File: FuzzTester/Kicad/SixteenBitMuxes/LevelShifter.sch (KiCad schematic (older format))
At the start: 6 parts, among them U22 4504, U23 4504, U24 4504

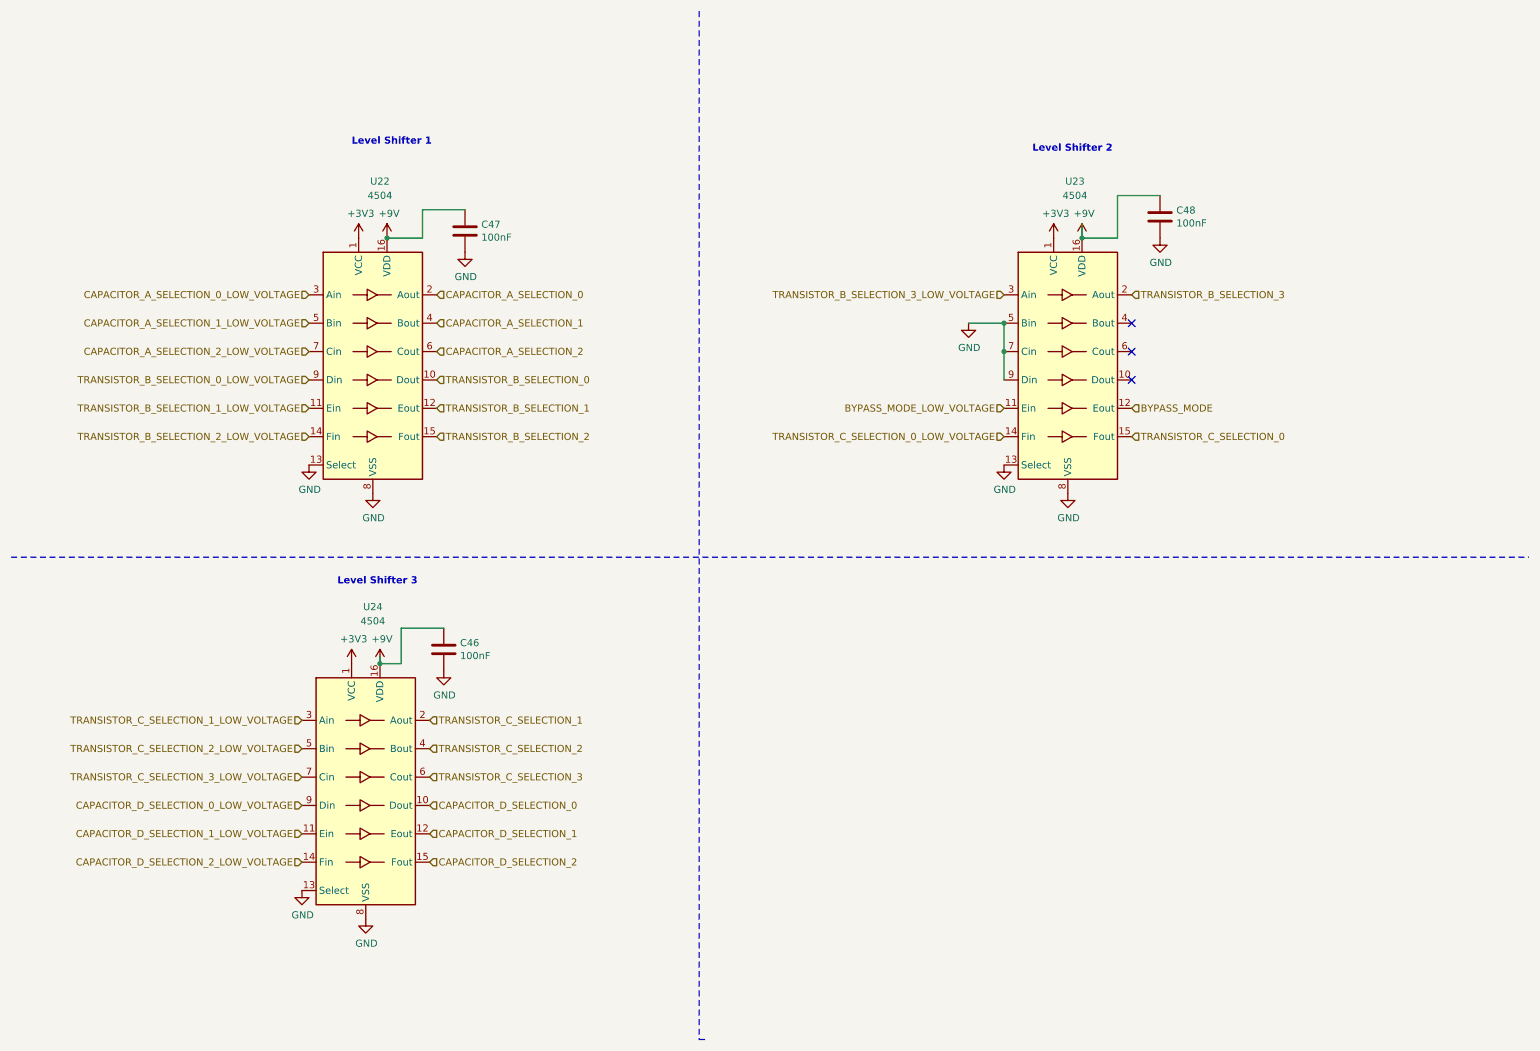
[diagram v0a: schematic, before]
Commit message: Removed shift registers
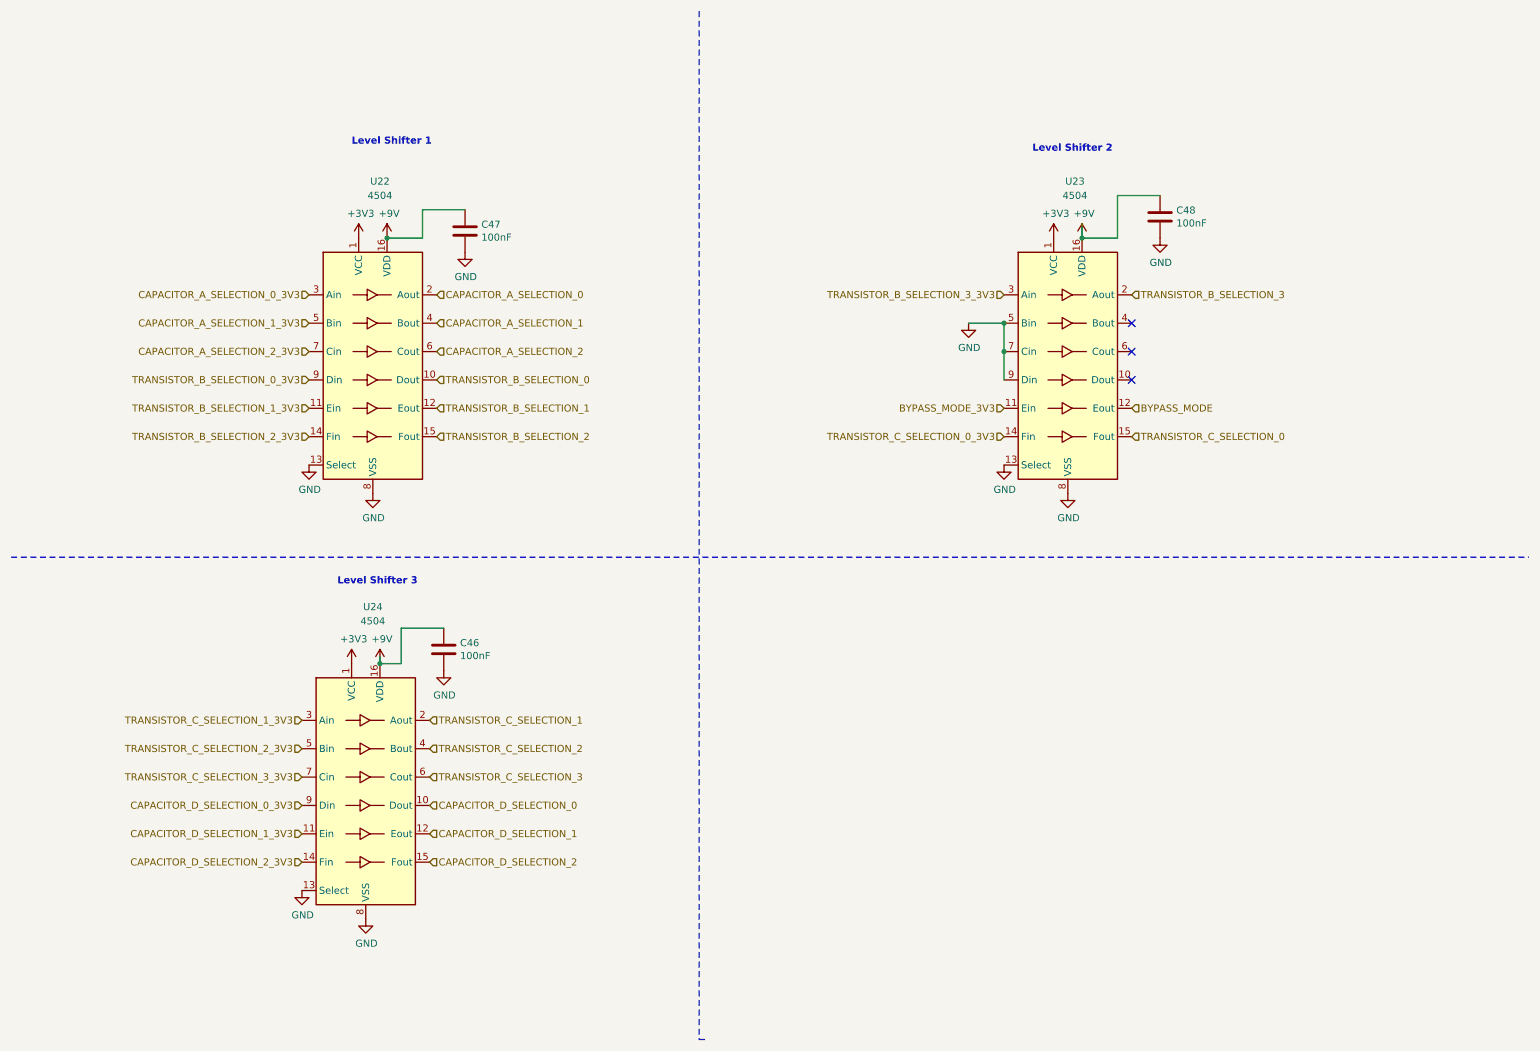
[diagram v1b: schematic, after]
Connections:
- net labels added: BYPASS_MODE_3V3, CAPACITOR_A_SELECTION_0_3V3, CAPACITOR_A_SELECTION_1_3V3, CAPACITOR_A_SELECTION_2_3V3, CAPACITOR_D_SELECTION_0_3V3, CAPACITOR_D_SELECTION_1_3V3, CAPACITOR_D_SELECTION_2_3V3, TRANSISTOR_B_SELECTION_0_3V3, TRANSISTOR_B_SELECTION_1_3V3, TRANSISTOR_B_SELECTION_2_3V3, TRANSISTOR_B_SELECTION_3_3V3, TRANSISTOR_C_SELECTION_0_3V3, TRANSISTOR_C_SELECTION_1_3V3, TRANSISTOR_C_SELECTION_2_3V3, TRANSISTOR_C_SELECTION_3_3V3
- net labels removed: BYPASS_MODE_LOW_VOLTAGE, CAPACITOR_A_SELECTION_0_LOW_VOLTAGE, CAPACITOR_A_SELECTION_1_LOW_VOLTAGE, CAPACITOR_A_SELECTION_2_LOW_VOLTAGE, CAPACITOR_D_SELECTION_0_LOW_VOLTAGE, CAPACITOR_D_SELECTION_1_LOW_VOLTAGE, CAPACITOR_D_SELECTION_2_LOW_VOLTAGE, TRANSISTOR_B_SELECTION_0_LOW_VOLTAGE, TRANSISTOR_B_SELECTION_1_LOW_VOLTAGE, TRANSISTOR_B_SELECTION_2_LOW_VOLTAGE, TRANSISTOR_B_SELECTION_3_LOW_VOLTAGE, TRANSISTOR_C_SELECTION_0_LOW_VOLTAGE, TRANSISTOR_C_SELECTION_1_LOW_VOLTAGE, TRANSISTOR_C_SELECTION_2_LOW_VOLTAGE, TRANSISTOR_C_SELECTION_3_LOW_VOLTAGE
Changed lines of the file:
@@
 $Descr A4 11693 8268
 encoding utf-8
-Sheet 11 11
+Sheet 11 9
 Title ""
 Date ""
@@
 	3250 5100 3100 5100
 Text HLabel 7500 3300 0    50   Input ~ 0
-BYPASS_MODE_LOW_VOLTAGE
+BYPASS_MODE_3V3
 Wire Wire Line
 	7250 2700 7500 2700
@@
 NoConn ~ 8400 3100
 Text HLabel 2600 2500 0    50   Input ~ 0
-CAPACITOR_A_SELECTION_0_LOW_VOLTAGE
+CAPACITOR_A_SELECTION_0_3V3
 Text HLabel 2600 2700 0    50   Input ~ 0
-CAPACITOR_A_SELECTION_1_LOW_VOLTAGE
+CAPACITOR_A_SELECTION_1_3V3
 Text HLabel 2600 2900 0    50   Input ~ 0
-CAPACITOR_A_SELECTION_2_LOW_VOLTAGE
+CAPACITOR_A_SELECTION_2_3V3
 Text HLabel 2600 3100 0    50   Input ~ 0
-TRANSISTOR_B_SELECTION_0_LOW_VOLTAGE
+TRANSISTOR_B_SELECTION_0_3V3
 Text HLabel 2600 3300 0    50   Input ~ 0
-TRANSISTOR_B_SELECTION_1_LOW_VOLTAGE
+TRANSISTOR_B_SELECTION_1_3V3
 Text HLabel 2600 3500 0    50   Input ~ 0
-TRANSISTOR_B_SELECTION_2_LOW_VOLTAGE
+TRANSISTOR_B_SELECTION_2_3V3
 Text HLabel 7500 2500 0    50   Input ~ 0
-TRANSISTOR_B_SELECTION_3_LOW_VOLTAGE
+TRANSISTOR_B_SELECTION_3_3V3
 Text HLabel 8400 2500 2    50   Input ~ 0
 TRANSISTOR_B_SELECTION_3
 Text HLabel 7500 3500 0    50   Input ~ 0
-TRANSISTOR_C_SELECTION_0_LOW_VOLTAGE
+TRANSISTOR_C_SELECTION_0_3V3
 Text HLabel 8400 3500 2    50   Input ~ 0
 TRANSISTOR_C_SELECTION_0
 Text HLabel 2550 6500 0    50   Input ~ 0
-CAPACITOR_D_SELECTION_2_LOW_VOLTAGE
+CAPACITOR_D_SELECTION_2_3V3
 Text HLabel 2550 6300 0    50   Input ~ 0
-CAPACITOR_D_SELECTION_1_LOW_VOLTAGE
+CAPACITOR_D_SELECTION_1_3V3
 Text HLabel 2550 6100 0    50   Input ~ 0
-CAPACITOR_D_SELECTION_0_LOW_VOLTAGE
+CAPACITOR_D_SELECTION_0_3V3
 Text HLabel 2550 5700 0    50   Input ~ 0
-TRANSISTOR_C_SELECTION_2_LOW_VOLTAGE
+TRANSISTOR_C_SELECTION_2_3V3
 Text HLabel 2550 5500 0    50   Input ~ 0
-TRANSISTOR_C_SELECTION_1_LOW_VOLTAGE
+TRANSISTOR_C_SELECTION_1_3V3
 Text HLabel 3450 5900 2    50   Input ~ 0
 TRANSISTOR_C_SELECTION_3
 Text HLabel 2550 5900 0    50   Input ~ 0
-TRANSISTOR_C_SELECTION_3_LOW_VOLTAGE
+TRANSISTOR_C_SELECTION_3_3V3
 $EndSCHEMATC

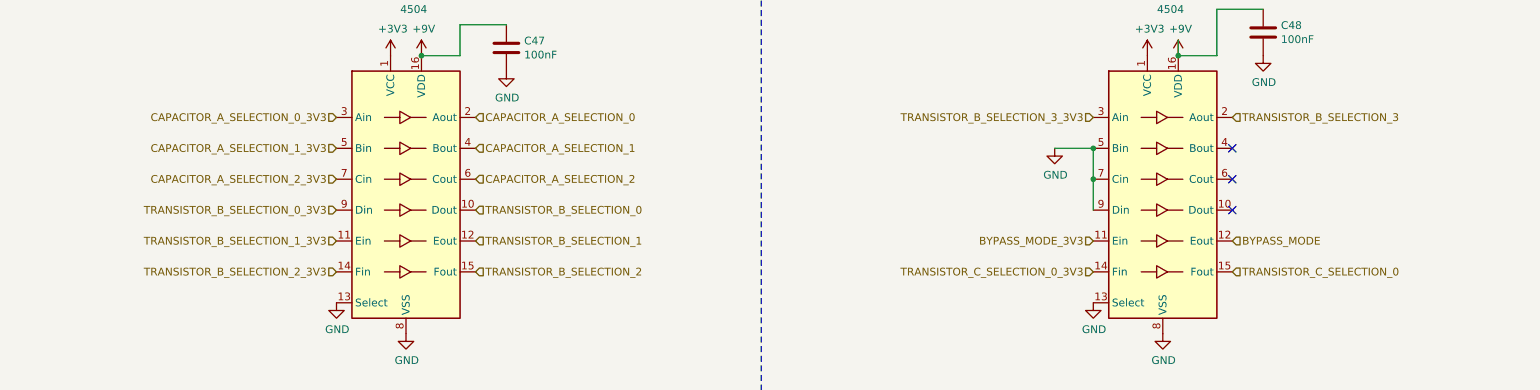
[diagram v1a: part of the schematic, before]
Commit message: Finished (but not beautiful) PCB without SPI and most 8 channel multiplexers.
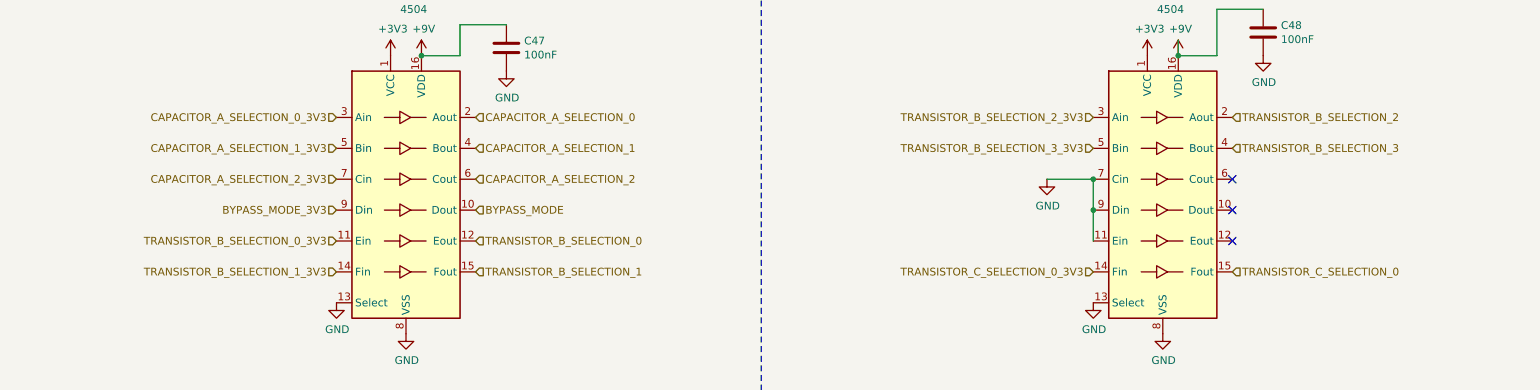
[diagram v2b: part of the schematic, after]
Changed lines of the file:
@@
 $Descr A4 11693 8268
 encoding utf-8
-Sheet 11 9
+Sheet 9 9
 Title ""
 Date ""
@@
 Text HLabel 3500 2900 2    50   Input ~ 0
 CAPACITOR_A_SELECTION_2
-Text HLabel 3500 3100 2    50   Input ~ 0
+Text HLabel 3500 3300 2    50   Input ~ 0
 TRANSISTOR_B_SELECTION_0
-Text HLabel 3500 3300 2    50   Input ~ 0
+Text HLabel 3500 3500 2    50   Input ~ 0
 TRANSISTOR_B_SELECTION_1
-Text HLabel 3500 3500 2    50   Input ~ 0
+Text HLabel 8400 2500 2    50   Input ~ 0
 TRANSISTOR_B_SELECTION_2
 $Comp
@@
 L power:GND #PWR0125
 U 1 1 5EDC2DD2
-P 7250 2700
-F 0 "#PWR0125" H 7250 2450 50  0001 C CNN
-F 1 "GND" H 7255 2527 50  0000 C CNN
-F 2 "" H 7250 2700 50  0001 C CNN
-F 3 "" H 7250 2700 50  0001 C CNN
-	1    7250 2700
+P 7200 2900
+F 0 "#PWR0125" H 7200 2650 50  0001 C CNN
+F 1 "GND" H 7205 2727 50  0000 C CNN
+F 2 "" H 7200 2900 50  0001 C CNN
+F 3 "" H 7200 2900 50  0001 C CNN
+	1    7200 2900
 	1    0    0    -1
 $EndComp
@@
 	1    0    0    -1
 $EndComp
-Text HLabel 8400 3300 2    50   Input ~ 0
+Text HLabel 3500 3100 2    50   Input ~ 0
 BYPASS_MODE
 $Comp
@@
 Wire Wire Line
 	3250 5100 3100 5100
-Text HLabel 7500 3300 0    50   Input ~ 0
+Text HLabel 2600 3100 0    50   Input ~ 0
 BYPASS_MODE_3V3
 Wire Wire Line
-	7250 2700 7500 2700
-Wire Wire Line
 	7500 3100 7500 2900
-Connection ~ 7500 2700
-Connection ~ 7500 2900
-Wire Wire Line
-	7500 2900 7500 2700
-NoConn ~ 8400 2700
 NoConn ~ 8400 2900
 NoConn ~ 8400 3100
@@
 Text HLabel 2600 2900 0    50   Input ~ 0
 CAPACITOR_A_SELECTION_2_3V3
-Text HLabel 2600 3100 0    50   Input ~ 0
+Text HLabel 2600 3300 0    50   Input ~ 0
 TRANSISTOR_B_SELECTION_0_3V3
-Text HLabel 2600 3300 0    50   Input ~ 0
+Text HLabel 2600 3500 0    50   Input ~ 0
 TRANSISTOR_B_SELECTION_1_3V3
-Text HLabel 2600 3500 0    50   Input ~ 0
+Text HLabel 7500 2500 0    50   Input ~ 0
 TRANSISTOR_B_SELECTION_2_3V3
-Text HLabel 7500 2500 0    50   Input ~ 0
+Text HLabel 7500 2700 0    50   Input ~ 0
 TRANSISTOR_B_SELECTION_3_3V3
-Text HLabel 8400 2500 2    50   Input ~ 0
+Text HLabel 8400 2700 2    50   Input ~ 0
 TRANSISTOR_B_SELECTION_3
 Text HLabel 7500 3500 0    50   Input ~ 0
@@
 Text HLabel 2550 5900 0    50   Input ~ 0
 TRANSISTOR_C_SELECTION_3_3V3
+Wire Wire Line
+	7200 2900 7500 2900
+Connection ~ 7500 2900
+Wire Wire Line
+	7500 3300 7500 3100
+Connection ~ 7500 3100
+NoConn ~ 8400 3300
 $EndSCHEMATC
